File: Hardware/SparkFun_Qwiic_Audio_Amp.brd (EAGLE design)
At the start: 43.2 x 25.4 mm, 71 parts, among them J1 QWIIC, J2 TRS_INPUT, J6 SCREW, U6 TPA2016D2RTJ

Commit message: Layout done v01
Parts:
- added C17, C4: 0.1uF, SparkFun-Capacitors:0402-TIGHT
- added C2: 10uF, SparkFun-Capacitors:0805
- added JP1: JP1, SparkFun-Jumpers:SMT-JUMPER_2_NO_SILK
- added LOGO6: SPECIAL_INSTRUCTIONS-ORDERING, SparkFun-Aesthetics:ORDERING_INSTRUCTIONS
- added TP1, TP2: (no value), SparkFun-Connectors:TP_15TH
- added U$18: (no value), output:#L#33
- added U$26: (no value), output:#VIN#30
- added U$27: (no value), output:#GND#31
- added U$28: (no value), output:#R#34
- added U$29: (no value), output:#GND#25
- added U$31, U$32: (no value), output:###40
- added U$33: (no value), output:SPEAKER_OUT37
- added U$34: (no value), output:AUDIO_IN39
- added U$35, U$36: (no value), output:###41
- added U$37: (no value), output:#LEFT#43
- added U$38: (no value), output:#RIGHT#44
- added U$39: (no value), output:#JP1#2
- added U$40: (no value), output:##SHDN##2
- C10, C11, C12, C9: device SparkFun-Passives:0402-CAP -> SparkFun-Capacitors:0402
- C13, C15: value 10uF -> 1.0uF; device SparkFun:EIA3216 -> SparkFun-Capacitors:0402-TIGHT
- C14, C16: device SparkFun:0402-CAP -> SparkFun-Capacitors:0402-TIGHT
- C5: value 1uF -> 1.0uF; device SparkFun:0603-CAP -> SparkFun-Capacitors:0402-TIGHT
- C6, C7, C8: value 1uF -> 1.0uF; device SparkFun:0402-CAP -> SparkFun-Capacitors:0402-TIGHT
- J4: device SparkFun-Connectors:1X02_2.54_SCREWTERM -> SparkFun-Connectors:SCREWTERMINAL-3.5MM-2
- L1, L2, L3, L4: value (none) -> 220Ω; device SparkFun-Passives:0805 -> SparkFun-Coils:0805
- R1: value 10k -> 100k
- R2, R3: value 4.7k -> 2.2k
- U$13: device output:#EN#13 -> output:##SHDN##3
- U6: value TPA2016D2RTJ -> TPA2016D2; device mike-temp:QFN-20-0.5MM -> temp:QFN-20-0.5MM
- moved LOGO2 17.3 mm to (31.1, 7.85), turned to 270 degrees
- moved FRAME2 7.41 mm to (-7.62, -20.3)
- moved U$16 6.99 mm to (35.2, 9.25)
- moved LOGO5 6.90 mm to (17.4, 2.97)
- moved U$14 6.81 mm to (35.2, 16.0)
- moved J4 3.67 mm to (33.2, 21.8), turned to 180 degrees
- moved U$4 2.97 mm to (15.1, 7.15)
- moved U$8 2.97 mm to (15.2, 5.63)
- moved U$7 2.97 mm to (15.4, 8.93)
- moved R5 1.70 mm to (29.0, 16.4), turned to 90 degrees
- moved C15 1.67 mm to (25.0, 13.3), turned to 0 degrees
- moved C13 1.58 mm to (25.1, 3.91), turned to 0 degrees
- moved U$13 1.54 mm to (6.91, 7.44), flipped to the bottom
- moved U$20 1.42 mm to (35.5, 23.6)
- moved LOGO1 1.15 mm to (12.8, 4.29)
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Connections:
- net SPKL+ renamed SPK_R_+
- net SPKL- renamed SPK_R_-
- net SPKR+ renamed SPK_L_+
- net SPKR- renamed SPK_L_-
- net 3.3V: now also JP1.1
- net GND: now also C13.2, C15.2, C17.2, C2.2, C4.2, J4.1; no longer C13.C, C15.C, J4.P1
- net SCL: now also TP1.1
- net SDA: now also TP2.1
- net SDZ: now also C4.1
- net VCC: now also C13.1, C15.1, C17.1, C2.1, J4.2, JP1.2; no longer C13.A, C15.A, J4.P2
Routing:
- net 3.3V: track 11.6 -> 13.3 mm
- net SDA: track 24.0 -> 24.9 mm
- net VCC: track 31.2 -> 32.0 mm, vias 2 -> 5
- net INR: track 8.84 -> 9.45 mm
- net N$25: track 2.32 -> 1.77 mm
- net SCL: track 18.1 -> 18.5 mm, vias 2 -> 1
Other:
- board text added: "1"
- board text added: "2"
- board text added: "3"
- board text added: "4"
- board text added: "4-Layer"
- board text added: "Board Thickness is 1.6mm"
- board text added: "HASL Finish"
- board text added: "UNITS: INCHES"

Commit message: swapped inner layers to correct (2=GND, 15=VCC)
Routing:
- added copper zone on layer 15, net VCC
- removed copper zone on layer 2, net VCC
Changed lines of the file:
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@@
 <drawing>
 <settings>
-<setting alwaysvectorfont="yes"/>
+<setting alwaysvectorfont="no"/>
 <setting verticaltext="up"/>
 </settings>
-<grid distance="0.05" unitdist="inch" unit="inch" style="lines" multiple="1" display="yes" altdistance="0.0001" altunitdist="inch" altunit="inch"/>
+<grid distance="0.05" unitdist="inch" unit="inch" style="lines" multiple="1" display="yes" altdistance="0.005" altunitdist="inch" altunit="inch"/>
 <layers>
-<layer number="1" name="Top" color="4" fill="1" visible="yes" active="yes"/>
-<layer number="16" name="Bottom" color="1" fill="1" visible="yes" active="yes"/>
-<layer number="17" name="Pads" color="2" fill="1" visible="yes" active="yes"/>
-<layer number="18" name="Vias" color="2" fill="1" visible="yes" active="yes"/>
-<layer number="19" name="Unrouted" color="6" fill="1" visible="yes" active="yes"/>
-<layer number="20" name="Dimension" color="24" fill="1" visible="yes" active="yes"/>
-<layer number="21" name="tPlace" color="16" fill="1" visible="yes" active="yes"/>
-<layer number="22" name="bPlace" color="14" fill="1" visible="yes" active="yes"/>
-<layer number="23" name="tOrigins" color="15" fill="1" visible="yes" active="yes"/>
-<layer number="24" name="bOrigins" color="15" fill="1" visible="yes" active="yes"/>
+<layer number="1" name="Top" color="4" fill="1" visible="no" active="yes"/>
+<layer number="16" name="Bottom" color="1" fill="1" visible="no" active="yes"/>
+<layer number="17" name="Pads" color="2" fill="1" visible="no" active="yes"/>
+<layer number="18" name="Vias" color="2" fill="1" visible="no" active="yes"/>
+<layer number="19" name="Unrouted" color="6" fill="1" visible="no" active="yes"/>
+<layer number="20" name="Dimension" color="24" fill="1" visible="no" active="yes"/>
+<layer number="21" name="tPlace" color="16" fill="1" visible="no" active="yes"/>
+<layer number="22" name="bPlace" color="14" fill="1" visible="no" active="yes"/>
+<layer number="23" name="tOrigins" color="15" fill="1" visible="no" active="yes"/>
+<layer number="24" name="bOrigins" color="15" fill="1" visible="no" active="yes"/>
 <layer number="25" name="tNames" color="7" fill="1" visible="no" active="yes"/>
 <layer number="26" name="bNames" color="7" fill="1" visible="no" active="yes"/>
@@
 <layer number="43" name="vRestrict" color="2" fill="10" visible="no" active="yes"/>
 <layer number="44" name="Drills" color="7" fill="1" visible="no" active="yes"/>
-<layer number="45" name="Holes" color="7" fill="1" visible="yes" active="yes"/>
+<layer number="45" name="Holes" color="7" fill="1" visible="no" active="yes"/>
 <layer number="46" name="Milling" color="3" fill="1" visible="no" active="yes"/>
 <layer number="47" name="Measures" color="7" fill="1" visible="no" active="yes"/>
 <layer number="48" name="Document" color="7" fill="1" visible="no" active="yes"/>
-<layer number="49" name="Reference" color="13" fill="1" visible="yes" active="yes"/>
+<layer number="49" name="Reference" color="13" fill="1" visible="no" active="yes"/>
 <layer number="50" name="dxf" color="7" fill="1" visible="no" active="yes"/>
-<layer number="51" name="tDocu" color="6" fill="1" visible="yes" active="yes"/>
+<layer number="51" name="tDocu" color="6" fill="1" visible="no" active="yes"/>
 <layer number="52" name="bDocu" color="7" fill="1" visible="no" active="yes"/>
 <layer number="91" name="Nets" color="2" fill="1" visible="no" active="no"/>
@@
 <layer number="13" name="Route13" color="21" fill="1" visible="no" active="no"/>
 <layer number="14" name="Route14" color="22" fill="1" visible="no" active="no"/>
-<layer number="15" name="Route15" color="23" fill="3" visible="no" active="yes"/>
+<layer number="15" name="Route15" color="23" fill="3" visible="yes" active="yes"/>
 <layer number="53" name="tGND_GNDA" color="7" fill="9" visible="no" active="no"/>
 <layer number="54" name="bGND_GNDA" color="1" fill="9" visible="no" active="no"/>
@@
 </element>
 <element name="U$39" library="output" package="#JP1#2" value="" x="21.0693" y="23.18511875" smashed="yes" rot="MR0"/>
-<element name="LOGO6" library="SparkFun-Aesthetics" package="ORDERING_INSTRUCTIONS" value="SPECIAL_INSTRUCTIONS-ORDERING" x="55.88" y="44.45" smashed="yes"/>
+<element name="LOGO6" library="SparkFun-Aesthetics" package="ORDERING_INSTRUCTIONS" value="SPECIAL_INSTRUCTIONS-ORDERING" x="55.88" y="44.45" smashed="yes">
+<attribute name="PROD_ID" value="PCB-17002" x="55.88" y="44.45" size="1.778" layer="27" display="off"/>
+</element>
 <element name="TP1" library="SparkFun-Connectors" package="TP_15TH" value="" x="21.59" y="21.59" smashed="yes"/>
 <element name="TP2" library="SparkFun-Connectors" package="TP_15TH" value="" x="21.59" y="17.78" smashed="yes"/>
@@
 <contactref element="R5" pad="1"/>
 <contactref element="J6" pad="1"/>
-<polygon width="0.2032" layer="15" isolate="0.3048">
-<vertex x="0" y="0"/>
-<vertex x="0" y="25.4"/>
-<vertex x="43.18" y="25.4"/>
-<vertex x="43.18" y="0"/>
-</polygon>
 <via x="32.22751875" y="12.799059375" extent="1-16" drill="0.3048"/>
 <via x="32.25291875" y="10.309859375" extent="1-16" drill="0.3048"/>
 <via x="32.2605375" y="6.322059375" extent="1-16" drill="0.3048"/>
 <via x="32.3240375" y="3.9116" extent="1-16" drill="0.3048"/>
-<polygon width="0.2032" layer="2" isolate="0.3048">
+<polygon width="0.2032" layer="15" isolate="0.3048">
 <vertex x="22.3012" y="9.92378125"/>
 <vertex x="22.3012" y="7.432040625"/>
@@
 <contactref element="C17" pad="2"/>
 <via x="18.97888125" y="11.88211875" extent="1-16" drill="0.3048"/>
+<polygon width="0.2032" layer="2" isolate="0.3048">
+<vertex x="0" y="0"/>
+<vertex x="0" y="25.4"/>
+<vertex x="43.18" y="25.4"/>
+<vertex x="43.18" y="0"/>
+</polygon>
 </signal>
 <signal name="SCL">
@@
 <contactref element="J4" pad="2"/>
 <contactref element="LED" pad="2"/>
-<polygon width="0.2032" layer="2" isolate="0.3048" rank="2">
-<vertex x="0" y="0"/>
-<vertex x="0" y="25.4"/>
-<vertex x="43.18" y="25.4"/>
-<vertex x="43.18" y="0"/>
-</polygon>
 <wire x1="18.605503125" y1="9.69988125" x2="18.605503125" y2="10.58418125" width="0.2032" layer="1"/>
 <wire x1="18.605503125" y1="10.58418125" x2="18.608040625" y2="10.58418125" width="0.2032" layer="1"/>
@@
 <wire x1="24.1808" y1="23.22321875" x2="24.704040625" y2="23.22321875" width="0.508" layer="16"/>
 <wire x1="24.704040625" y1="23.22321875" x2="25.463503125" y2="22.46375625" width="0.508" layer="16"/>
+<polygon width="0.2032" layer="15" isolate="0.3048" rank="2">
+<vertex x="0" y="0"/>
+<vertex x="0" y="25.4"/>
+<vertex x="43.18" y="25.4"/>
+<vertex x="43.18" y="0"/>
+</polygon>
 </signal>
 <signal name="INL_SCRWPN">

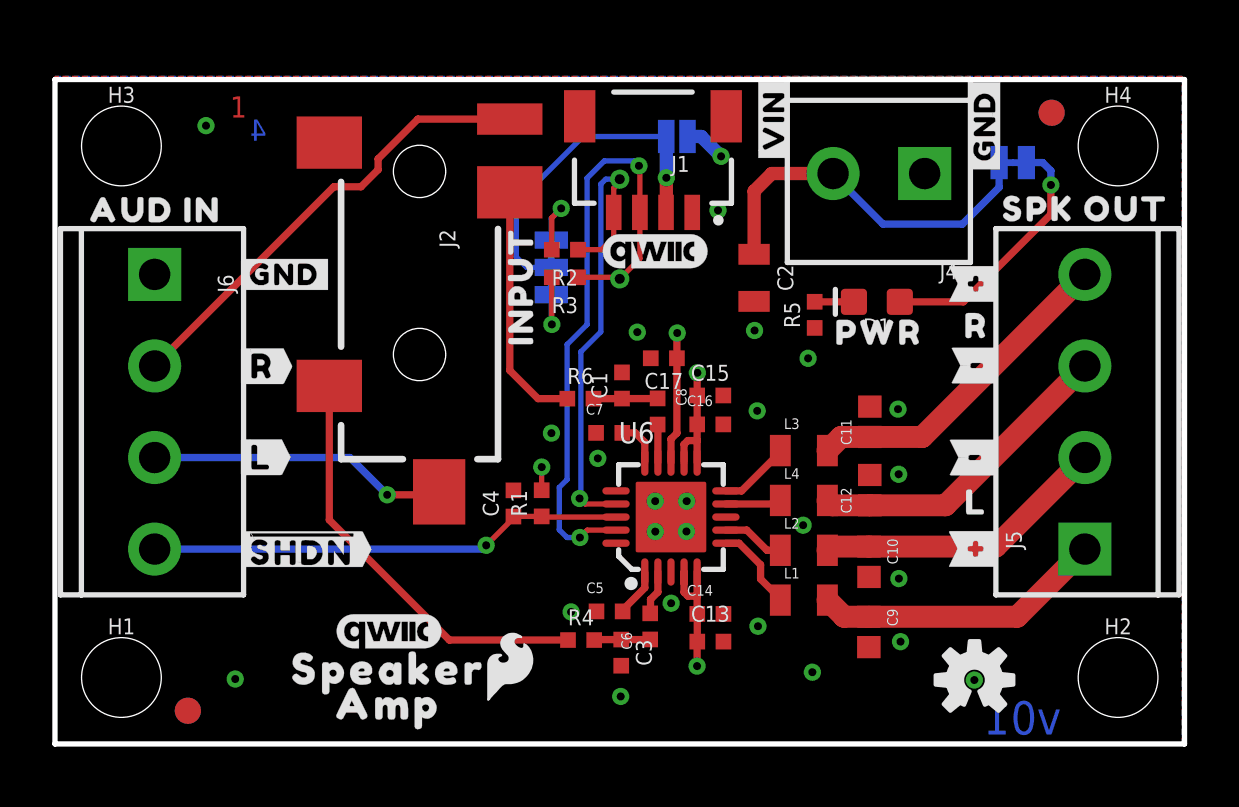
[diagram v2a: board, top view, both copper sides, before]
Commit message: schematic cleanup and minor board fixes
-more gnd vias
-drc approvals
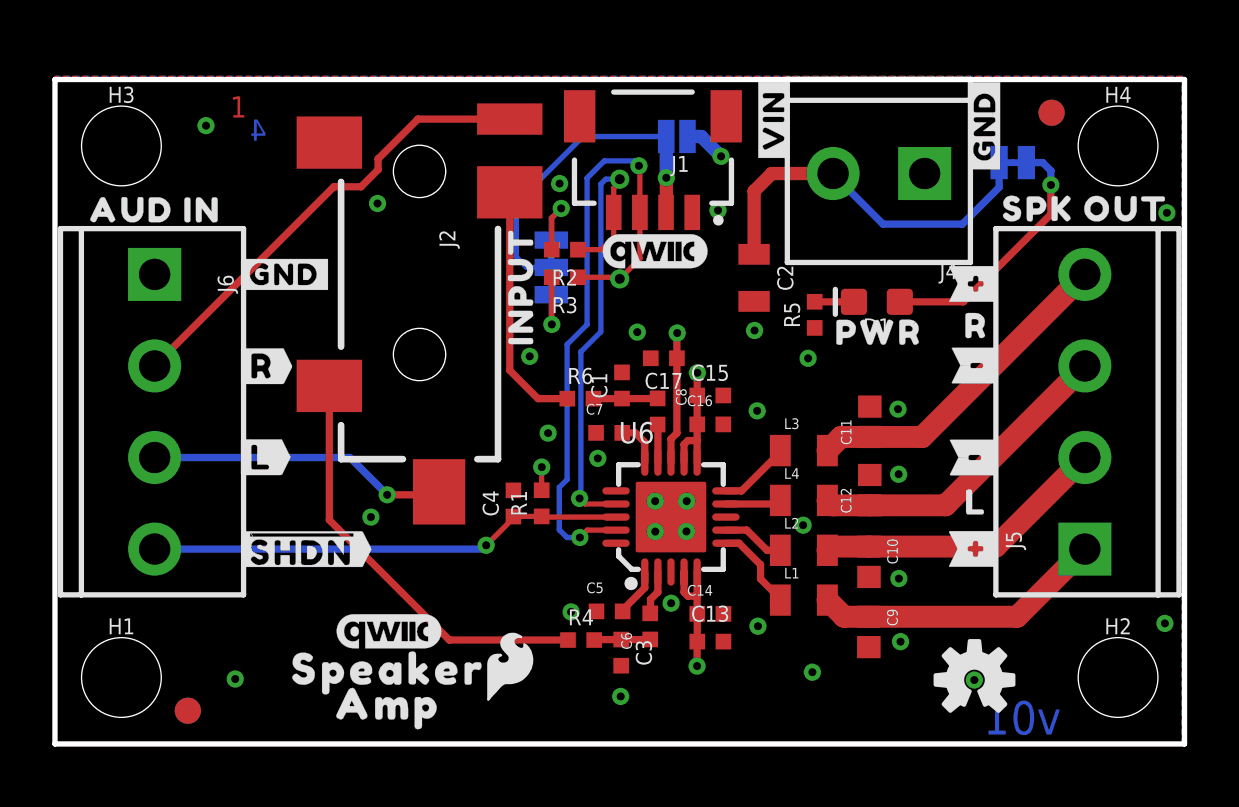
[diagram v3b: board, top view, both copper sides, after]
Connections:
- net SDZ renamed !SDZ!
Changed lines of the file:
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@@
 <drawing>
 <settings>
-<setting alwaysvectorfont="no"/>
+<setting alwaysvectorfont="yes"/>
 <setting verticaltext="up"/>
 </settings>
-<grid distance="0.05" unitdist="inch" unit="inch" style="lines" multiple="1" display="yes" altdistance="0.005" altunitdist="inch" altunit="inch"/>
+<grid distance="0.05" unitdist="inch" unit="inch" style="lines" multiple="1" display="yes" altdistance="0.001" altunitdist="inch" altunit="inch"/>
 <layers>
-<layer number="1" name="Top" color="4" fill="1" visible="no" active="yes"/>
-<layer number="16" name="Bottom" color="1" fill="1" visible="no" active="yes"/>
-<layer number="17" name="Pads" color="2" fill="1" visible="no" active="yes"/>
-<layer number="18" name="Vias" color="2" fill="1" visible="no" active="yes"/>
-<layer number="19" name="Unrouted" color="6" fill="1" visible="no" active="yes"/>
-<layer number="20" name="Dimension" color="24" fill="1" visible="no" active="yes"/>
-<layer number="21" name="tPlace" color="16" fill="1" visible="no" active="yes"/>
-<layer number="22" name="bPlace" color="14" fill="1" visible="no" active="yes"/>
-<layer number="23" name="tOrigins" color="15" fill="1" visible="no" active="yes"/>
-<layer number="24" name="bOrigins" color="15" fill="1" visible="no" active="yes"/>
+<layer number="1" name="Top" color="4" fill="1" visible="yes" active="yes"/>
+<layer number="16" name="Bottom" color="1" fill="1" visible="yes" active="yes"/>
+<layer number="17" name="Pads" color="2" fill="1" visible="yes" active="yes"/>
+<layer number="18" name="Vias" color="2" fill="1" visible="yes" active="yes"/>
+<layer number="19" name="Unrouted" color="6" fill="1" visible="yes" active="yes"/>
+<layer number="20" name="Dimension" color="24" fill="1" visible="yes" active="yes"/>
+<layer number="21" name="tPlace" color="16" fill="1" visible="yes" active="yes"/>
+<layer number="22" name="bPlace" color="14" fill="1" visible="yes" active="yes"/>
+<layer number="23" name="tOrigins" color="15" fill="1" visible="yes" active="yes"/>
+<layer number="24" name="bOrigins" color="15" fill="1" visible="yes" active="yes"/>
 <layer number="25" name="tNames" color="7" fill="1" visible="no" active="yes"/>
 <layer number="26" name="bNames" color="7" fill="1" visible="no" active="yes"/>
@@
 <layer number="43" name="vRestrict" color="2" fill="10" visible="no" active="yes"/>
 <layer number="44" name="Drills" color="7" fill="1" visible="no" active="yes"/>
-<layer number="45" name="Holes" color="7" fill="1" visible="no" active="yes"/>
+<layer number="45" name="Holes" color="7" fill="1" visible="yes" active="yes"/>
 <layer number="46" name="Milling" color="3" fill="1" visible="no" active="yes"/>
 <layer number="47" name="Measures" color="7" fill="1" visible="no" active="yes"/>
 <layer number="48" name="Document" color="7" fill="1" visible="no" active="yes"/>
-<layer number="49" name="Reference" color="13" fill="1" visible="no" active="yes"/>
+<layer number="49" name="Reference" color="13" fill="1" visible="yes" active="yes"/>
 <layer number="50" name="dxf" color="7" fill="1" visible="no" active="yes"/>
-<layer number="51" name="tDocu" color="6" fill="1" visible="no" active="yes"/>
+<layer number="51" name="tDocu" color="6" fill="1" visible="yes" active="yes"/>
 <layer number="52" name="bDocu" color="7" fill="1" visible="no" active="yes"/>
 <layer number="91" name="Nets" color="2" fill="1" visible="no" active="no"/>
@@
 <layer number="13" name="Route13" color="21" fill="1" visible="no" active="no"/>
 <layer number="14" name="Route14" color="22" fill="1" visible="no" active="no"/>
-<layer number="15" name="Route15" color="23" fill="3" visible="yes" active="yes"/>
+<layer number="15" name="Route15" color="23" fill="3" visible="no" active="yes"/>
 <layer number="53" name="tGND_GNDA" color="7" fill="9" visible="no" active="no"/>
 <layer number="54" name="bGND_GNDA" color="1" fill="9" visible="no" active="no"/>
@@
 <via x="26.7436625" y="15.80641875" extent="1-16" drill="0.3048"/>
 <contactref element="C17" pad="2"/>
-<via x="18.97888125" y="11.88211875" extent="1-16" drill="0.3048"/>
+<via x="18.85188125" y="11.88211875" extent="1-16" drill="0.3048"/>
 <polygon width="0.2032" layer="2" isolate="0.3048">
 <vertex x="0" y="0"/>
@@
 <vertex x="43.18" y="0"/>
 </polygon>
+<via x="42.5069" y="20.304759375" extent="1-16" drill="0.3048"/>
+<via x="42.4307" y="4.607559375" extent="1-16" drill="0.3048"/>
+<via x="19.2913" y="21.422359375" extent="1-16" drill="0.3048"/>
+<via x="12.3317" y="20.660359375" extent="1-16" drill="0.3048"/>
+<via x="18.1483" y="14.818359375" extent="1-16" drill="0.3048"/>
+<via x="12.0777" y="8.671559375" extent="1-16" drill="0.3048"/>
 </signal>
 <signal name="SCL">
@@
 <wire x1="22.750021875" y1="3.989959375" x2="21.64588125" y2="3.989959375" width="0.2794" layer="1"/>
 </signal>
-<signal name="SDZ">
+<signal name="!SDZ!">
 <contactref element="U6" pad="18"/>
 <contactref element="R1" pad="1"/>
@@
 </signals>
 <mfgpreviewcolors>
-<mfgpreviewcolor name="soldermaskcolor" color="0xC8AA0000"/>
+<mfgpreviewcolor name="soldermaskcolor" color="0xC8FF0000"/>
 <mfgpreviewcolor name="silkscreencolor" color="0xFFFEFEFE"/>
 <mfgpreviewcolor name="backgroundcolor" color="0xFF282828"/>
